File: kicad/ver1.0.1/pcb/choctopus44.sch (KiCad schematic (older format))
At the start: 94 parts, among them SW1 SW_PUSH, SW10 SW_PUSH, SW11 SW_PUSH, SW12 SW_PUSH, SW13 SW_PUSH, SW14 SW_PUSH, SW15 SW_PUSH, SW16 SW_PUSH, SW17 SW_PUSH, SW18 SW_PUSH, SW19 SW_PUSH, SW2 SW_PUSH, SW20 SW_PUSH, SW21 SW_PUSH, SW22 SW_PUSH, SW23 SW_PUSH, SW24 SW_PUSH, SW25 SW_PUSH, SW26 SW_PUSH, SW27 SW_PUSH, SW28 SW_PUSH, SW29 SW_PUSH, SW3 SW_PUSH, SW30 SW_PUSH, SW31 SW_PUSH, SW32 SW_PUSH, SW33 SW_PUSH, SW34 SW_PUSH, SW35 SW_PUSH, SW36 SW_PUSH, SW37 SW_PUSH, SW38 SW_PUSH, SW39 SW_PUSH, SW4 SW_PUSH, SW40 SW_PUSH, SW41 SW_PUSH, SW42 SW_PUSH, SW43 SW_PUSH, SW44 SW_PUSH, SW45 Rotary_Encoder_Switch, SW5 SW_PUSH, SW6 SW_PUSH, SW7 SW_PUSH, SW8 SW_PUSH, SW9 SW_PUSH, U1 ProMicro

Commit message: sorted schematic
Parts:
- removed RESET1: SW_PUSH, Button_Switch_THT:SW_TH_Tactile_Omron_B3F-10xx, symbol Switch:SW_DPST
- added RESET1: SW_Push_Dual, Button_Switch_THT:SW_TH_Tactile_Omron_B3F-10xx, symbol Switch:SW_Push_Dual
- SW_PWR1: symbol Switch:SW_DPST -> Switch:SW_Push_DPDT
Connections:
- net +BATT: now also SW_PWR1.5 (B); no longer SW_PWR1.1
- net -BATT: now also SW_PWR1.2 (B); no longer SW_PWR1.3
- net GND: now also RESET1.2, RESET1.4
- net reset: now also RESET1.1, RESET1.3
- net at BT1.2 (-): now also SW_PWR1.4 (A); no longer SW_PWR1.2
- net at BT1.1 (+): now also SW_PWR1.1 (A); no longer SW_PWR1.4
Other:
- moved on the sheet: BT1
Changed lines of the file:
@@
 Text GLabel 3250 7050 0    50   Input ~ 0
 reset
-$Comp
-L Switch:SW_DPST RESET1
-U 1 1 5DD41146
-P 3550 7050
-F 0 "RESET1" H 3550 7305 50  0000 C CNN
-F 1 "SW_PUSH" H 3550 7214 50  0000 C CNN
-F 2 "Button_Switch_THT:SW_TH_Tactile_Omron_B3F-10xx" H 3550 7050 50  0001 C CNN
-F 3 "" H 3550 7050 50  0000 C CNN
-	1    3550 7050
-	1    0    0    -1
-$EndComp
 Wire Wire Line
 	3750 1050 3750 1350
@@
 	8350 5550 9350 5550
 $Comp
-L Switch:SW_DPST SW_PWR1
-U 1 1 60DF3383
-P 1800 3700
-F 0 "SW_PWR1" H 1800 4025 50  0000 C CNN
-F 1 "SW_DPST" H 1800 3934 50  0000 C CNN
-F 2 "Button_Switch_THT:SW_E-Switch_EG1271_DPDT" H 1800 3700 50  0001 C CNN
-F 3 "~" H 1800 3700 50  0001 C CNN
-	1    1800 3700
-	1    0    0    -1
-$EndComp
-$Comp
 L power:+BATT #PWR0102
 U 1 1 60DF5849
-P 1200 3850
-F 0 "#PWR0102" H 1200 3700 50  0001 C CNN
-F 1 "+BATT" H 1215 4023 50  0000 C CNN
-F 2 "Connector_PinHeader_2.00mm:PinHeader_1x01_P2.00mm_Vertical" H 1200 3850 50  0001 C CNN
-F 3 "" H 1200 3850 50  0001 C CNN
-	1    1200 3850
-	1    0    0    -1
+P 1550 3950
+F 0 "#PWR0102" H 1550 3800 50  0001 C CNN
+F 1 "+BATT" H 1565 4123 50  0000 C CNN
+F 2 "Connector_PinHeader_2.00mm:PinHeader_1x01_P2.00mm_Vertical" H 1550 3950 50  0001 C CNN
+F 3 "" H 1550 3950 50  0001 C CNN
+	1    1550 3950
+	0    -1   -1   0
 $EndComp
 $Comp
 L power:-BATT #PWR0103
 U 1 1 60DF6A16
-P 1200 3550
-F 0 "#PWR0103" H 1200 3400 50  0001 C CNN
-F 1 "-BATT" H 1215 3723 50  0000 C CNN
-F 2 "Connector_PinHeader_2.00mm:PinHeader_1x01_P2.00mm_Vertical" H 1200 3550 50  0001 C CNN
-F 3 "" H 1200 3550 50  0001 C CNN
-	1    1200 3550
-	1    0    0    -1
+P 1550 3550
+F 0 "#PWR0103" H 1550 3400 50  0001 C CNN
+F 1 "-BATT" H 1565 3723 50  0000 C CNN
+F 2 "Connector_PinHeader_2.00mm:PinHeader_1x01_P2.00mm_Vertical" H 1550 3550 50  0001 C CNN
+F 3 "" H 1550 3550 50  0001 C CNN
+	1    1550 3550
+	0    -1   -1   0
 $EndComp
 $Comp
 L Device:Battery_Cell BT1
 U 1 1 60DF8FE8
-P 2350 3750
-F 0 "BT1" H 2468 3846 50  0000 L CNN
-F 1 "Battery_Cell" H 2468 3755 50  0000 L CNN
-F 2 "Connector_PinHeader_2.00mm:PinHeader_1x02_P2.00mm_Vertical" V 2350 3810 50  0001 C CNN
-F 3 "~" V 2350 3810 50  0001 C CNN
-	1    2350 3750
-	1    0    0    -1
-$EndComp
-Wire Wire Line
-	2350 3550 2000 3550
-Wire Wire Line
-	2000 3550 2000 3600
-Wire Wire Line
-	2350 3850 2000 3850
-Wire Wire Line
-	2000 3850 2000 3800
-Wire Wire Line
-	1600 3800 1600 3850
-Wire Wire Line
-	1600 3850 1200 3850
-Wire Wire Line
-	1200 3550 1600 3550
-Wire Wire Line
-	1600 3550 1600 3600
+P 2350 3700
+F 0 "BT1" H 2468 3796 50  0000 L CNN
+F 1 "Battery_Cell" H 2468 3705 50  0000 L CNN
+F 2 "Connector_PinHeader_2.00mm:PinHeader_1x02_P2.00mm_Vertical" V 2350 3760 50  0001 C CNN
+F 3 "~" V 2350 3760 50  0001 C CNN
+	1    2350 3700
+	1    0    0    -1
+$EndComp
 Wire Wire Line
 	3250 7050 3350 7050
@@
 Wire Wire Line
 	6850 5900 6750 5900
+$Comp
+L Switch:SW_Push_DPDT SW_PWR1
+U 1 1 60DF3383
+P 1800 3750
+F 0 "SW_PWR1" H 1750 4250 50  0000 C CNN
+F 1 "SW_DPST" H 1750 4150 50  0000 C CNN
+F 2 "Button_Switch_THT:SW_E-Switch_EG1271_DPDT" H 1800 3750 50  0001 C CNN
+F 3 "~" H 1800 3750 50  0001 C CNN
+	1    1800 3750
+	1    0    0    -1
+$EndComp
+Wire Wire Line
+	2000 3450 2350 3450
+Wire Wire Line
+	2350 3450 2350 3500
+Wire Wire Line
+	2000 3850 2350 3850
+Wire Wire Line
+	2350 3850 2350 3800
+Wire Wire Line
+	1550 3950 1600 3950
+Wire Wire Line
+	1550 3550 1600 3550
+$Comp
+L Switch:SW_Push_Dual RESET1
+U 1 1 618A4AC7
+P 3550 6950
+F 0 "RESET1" H 3550 7235 50  0000 C CNN
+F 1 "SW_Push_Dual" H 3550 7144 50  0000 C CNN
+F 2 "Button_Switch_THT:SW_TH_Tactile_Omron_B3F-10xx" H 3550 7150 50  0001 C CNN
+F 3 "~" H 3550 7150 50  0001 C CNN
+	1    3550 6950
+	1    0    0    -1
+$EndComp
 $EndSCHEMATC

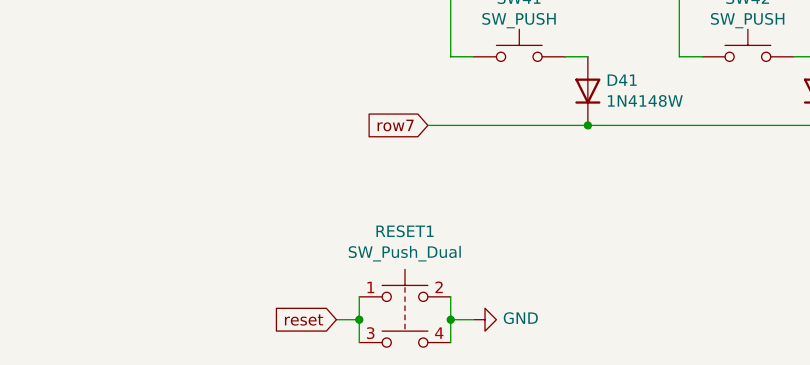
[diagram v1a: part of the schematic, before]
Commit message: sorted PCB *and schematic some more*
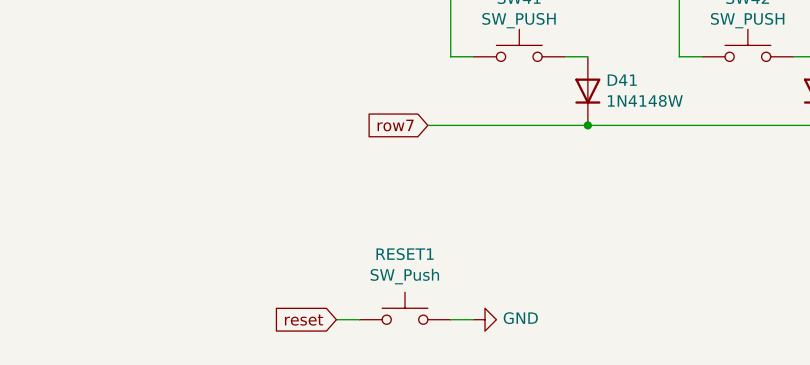
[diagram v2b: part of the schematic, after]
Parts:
- removed RESET1: SW_Push_Dual, Button_Switch_THT:SW_TH_Tactile_Omron_B3F-10xx, symbol Switch:SW_Push_Dual
- added RESET1: SW_Push, Button_Switch_THT:SW_PUSH_6mm, symbol Switch:SW_Push
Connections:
- net GND: now also RESET1.2
- net reset: now also RESET1.1
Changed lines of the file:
@@
 	3250 7050 3350 7050
 Wire Wire Line
-	3350 7050 3350 6950
-Wire Wire Line
-	3350 7050 3350 7150
-Connection ~ 3350 7050
-Wire Wire Line
-	3750 6950 3750 7050
-Wire Wire Line
 	3750 7050 3850 7050
-Wire Wire Line
-	3750 7150 3750 7050
-Connection ~ 3750 7050
 Wire Wire Line
 	3750 5900 3850 5900
@@
 	1550 3550 1600 3550
 $Comp
-L Switch:SW_Push_Dual RESET1
-U 1 1 618A4AC7
-P 3550 6950
-F 0 "RESET1" H 3550 7235 50  0000 C CNN
-F 1 "SW_Push_Dual" H 3550 7144 50  0000 C CNN
-F 2 "Button_Switch_THT:SW_TH_Tactile_Omron_B3F-10xx" H 3550 7150 50  0001 C CNN
-F 3 "~" H 3550 7150 50  0001 C CNN
-	1    3550 6950
+L Switch:SW_Push RESET1
+U 1 1 618CBE5E
+P 3550 7050
+F 0 "RESET1" H 3550 7335 50  0000 C CNN
+F 1 "SW_Push" H 3550 7244 50  0000 C CNN
+F 2 "Button_Switch_THT:SW_PUSH_6mm" H 3550 7250 50  0001 C CNN
+F 3 "~" H 3550 7250 50  0001 C CNN
+	1    3550 7050
 	1    0    0    -1
 $EndComp
